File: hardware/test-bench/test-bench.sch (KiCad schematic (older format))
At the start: 34 parts, among them J1 Conn_Mem_Ext, J2 Conn_Reg, J3 SWD, J4 Conn_Mem, J5 FTDI, J6 Conn_Power, SW1 SW_Push_4pin, SW2 SW_Push_4pin, U1 STM32G030F6, U2 MCP23S17_SS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

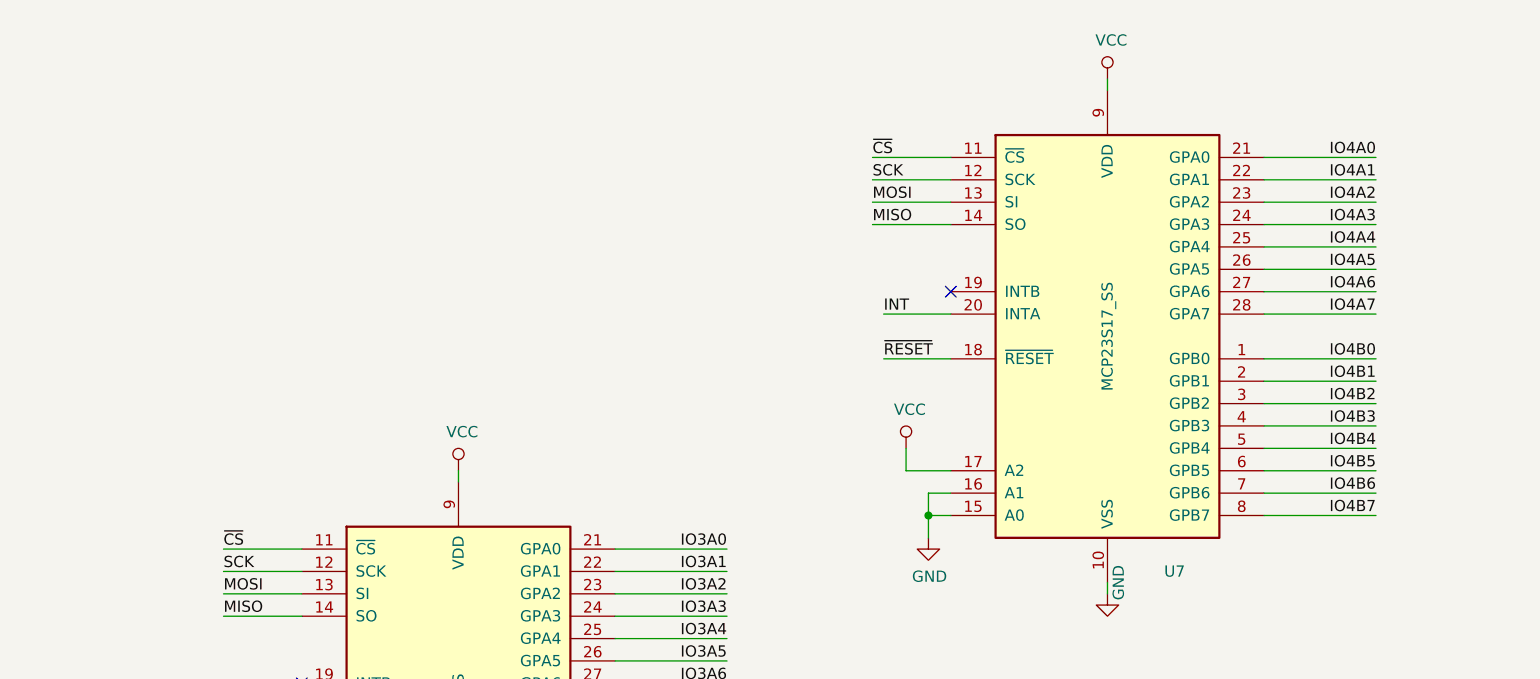
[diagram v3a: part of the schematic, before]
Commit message: Added test points
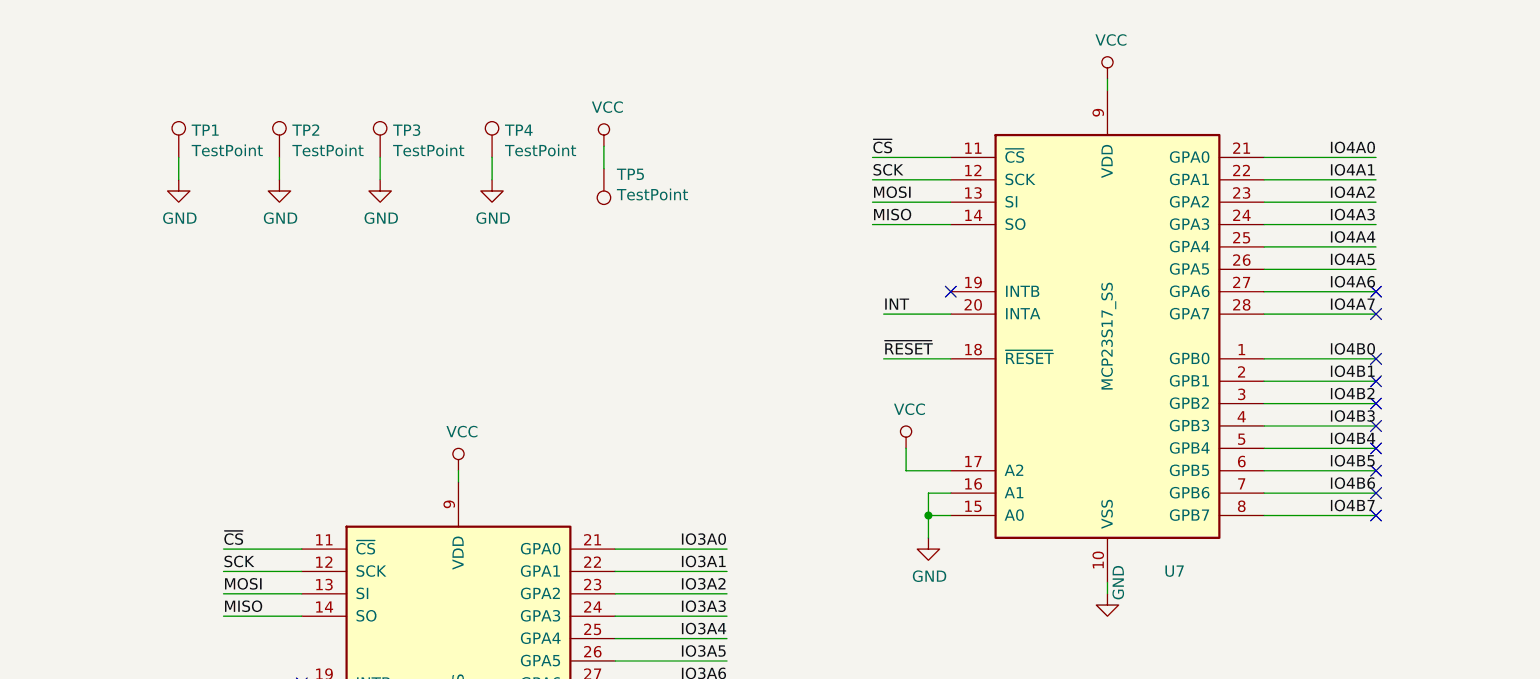
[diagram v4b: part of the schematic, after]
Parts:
- added TP1, TP2, TP3, TP4: TestPoint, TestPoint:TestPoint_THTPad_D2.0mm_Drill1.0mm, symbol Connector:TestPoint
- added TP5: TestPoint, TestPoint:TestPoint_Pad_2.0x2.0mm, symbol Connector:TestPoint
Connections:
- net GND: now also TP1.1, TP2.1, TP3.1, TP4.1
- net VCC: now also TP5.1
- no-connect marks 20 -> 30

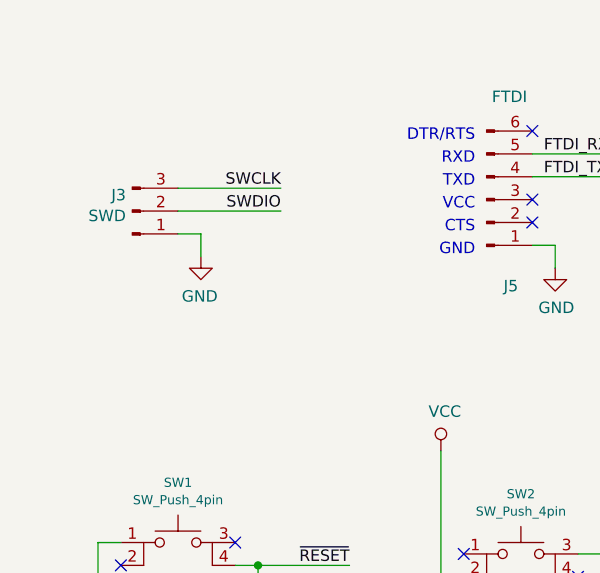
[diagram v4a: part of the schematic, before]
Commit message: Add J-LINK 10-pin SWD header
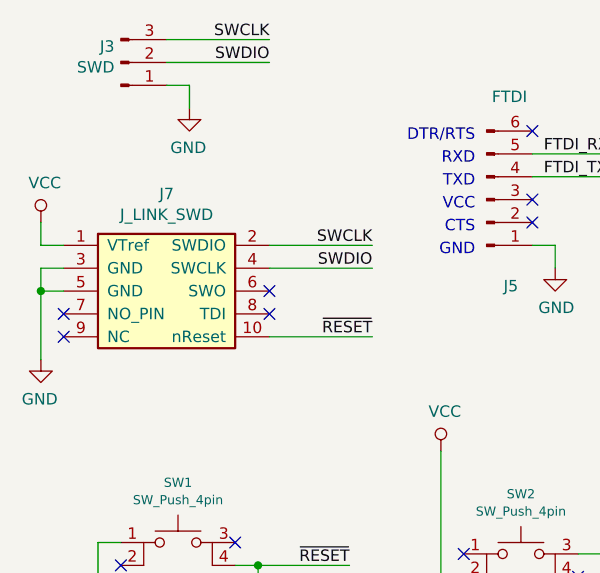
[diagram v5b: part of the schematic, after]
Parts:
- added J7: J_LINK_SWD, Connector_PinHeader_1.27mm:PinHeader_2x05_P1.27mm_Vertical_SMD, symbol riscv-serial:J_LINK_SWD
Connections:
- net GND: now also J7.3 (GND), J7.5 (GND)
- net SWCLK: now also J7.2 (SWDIO)
- net SWDIO: now also J7.4 (SWCLK)
- net VCC: now also J7.1 (VTref)
- net ~RESET: now also J7.10 (nReset)
- no-connect marks 30 -> 34
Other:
- moved on the sheet: J3
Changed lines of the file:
@@
 L Connector:Conn_01x03_Male J3
 U 1 1 5F42A36C
-P 1050 1550
-F 0 "J3" H 1022 1480 50  0000 R CNN
-F 1 "SWD" H 1022 1571 50  0000 R CNN
-F 2 "Connector_PinHeader_2.54mm:PinHeader_1x03_P2.54mm_Vertical" H 1050 1550 50  0001 C CNN
-F 3 "~" H 1050 1550 50  0001 C CNN
-	1    1050 1550
+P 1000 900
+F 0 "J3" H 972 830 50  0000 R CNN
+F 1 "SWD" H 972 921 50  0000 R CNN
+F 2 "Connector_PinHeader_2.54mm:PinHeader_1x03_P2.54mm_Vertical" H 1000 900 50  0001 C CNN
+F 3 "~" H 1000 900 50  0001 C CNN
+	1    1000 900
 	1    0    0    1
 $EndComp
@@
 L power:GND #PWR?
 U 1 1 5F43A491
-P 1350 1750
-F 0 "#PWR?" H 1350 1500 50  0001 C CNN
-F 1 "GND" H 1355 1577 50  0000 C CNN
-F 2 "" H 1350 1750 50  0001 C CNN
-F 3 "" H 1350 1750 50  0001 C CNN
-	1    1350 1750
+P 1300 1100
+F 0 "#PWR?" H 1300 850 50  0001 C CNN
+F 1 "GND" H 1305 927 50  0000 C CNN
+F 2 "" H 1300 1100 50  0001 C CNN
+F 3 "" H 1300 1100 50  0001 C CNN
+	1    1300 1100
 	-1   0    0    -1
 $EndComp
 Wire Wire Line
-	1250 1650 1350 1650
-Wire Wire Line
-	1350 1650 1350 1750
-Wire Wire Line
-	1250 1550 1700 1550
-Wire Wire Line
-	1250 1450 1700 1450
-Text Label 1700 1550 2    50   ~ 0
+	1200 1000 1300 1000
+Wire Wire Line
+	1300 1000 1300 1100
+Wire Wire Line
+	1200 900  1650 900
+Wire Wire Line
+	1200 800  1650 800
+Text Label 1650 900  2    50   ~ 0
 SWDIO
-Text Label 1700 1450 2    50   ~ 0
+Text Label 1650 800  2    50   ~ 0
 SWCLK
 $Comp
@@
 NoConn ~ 15100 3000
 NoConn ~ 15100 3100
+$Comp
+L riscv-serial:J_LINK_SWD J7
+U 1 1 5F4D5DF0
+P 1200 1900
+F 0 "J7" H 1200 2325 50  0000 C CNN
+F 1 "J_LINK_SWD" H 1200 2234 50  0000 C CNN
+F 2 "Connector_PinHeader_1.27mm:PinHeader_2x05_P1.27mm_Vertical_SMD" H 1200 1900 50  0001 C CNN
+F 3 "~" H 1200 1900 50  0001 C CNN
+	1    1200 1900
+	1    0    0    -1
+$EndComp
+Wire Wire Line
+	1650 1800 2100 1800
+Wire Wire Line
+	1650 1700 2100 1700
+Text Label 2100 1800 2    50   ~ 0
+SWDIO
+Text Label 2100 1700 2    50   ~ 0
+SWCLK
+$Comp
+L power:VCC #PWR?
+U 1 1 5F542329
+P 650 1600
+F 0 "#PWR?" H 650 1450 50  0001 C CNN
+F 1 "VCC" H 667 1773 50  0000 C CNN
+F 2 "" H 650 1600 50  0001 C CNN
+F 3 "" H 650 1600 50  0001 C CNN
+	1    650  1600
+	1    0    0    -1
+$EndComp
+Wire Wire Line
+	650  1600 650  1700
+Wire Wire Line
+	650  1700 750  1700
+NoConn ~ 750  2000
+NoConn ~ 750  2100
+NoConn ~ 1650 2000
+NoConn ~ 1650 1900
+$Comp
+L power:GND #PWR?
+U 1 1 5F5F9065
+P 650 2200
+F 0 "#PWR?" H 650 1950 50  0001 C CNN
+F 1 "GND" H 655 2027 50  0000 C CNN
+F 2 "" H 650 2200 50  0001 C CNN
+F 3 "" H 650 2200 50  0001 C CNN
+	1    650  2200
+	-1   0    0    -1
+$EndComp
+Wire Wire Line
+	750  1800 650  1800
+Wire Wire Line
+	650  1800 650  1900
+Wire Wire Line
+	750  1900 650  1900
+Connection ~ 650  1900
+Wire Wire Line
+	650  1900 650  2200
+Text Label 2100 2100 2    50   ~ 0
+~RESET
+Wire Wire Line
+	2100 2100 1650 2100
 $EndSCHEMATC

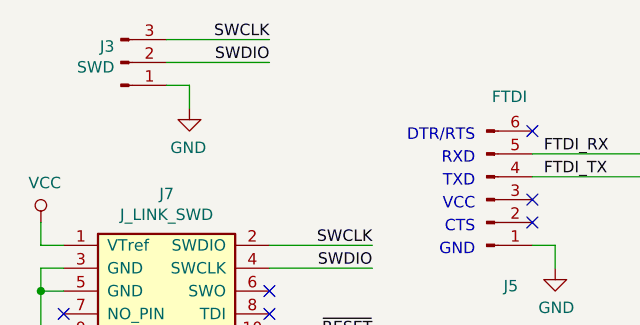
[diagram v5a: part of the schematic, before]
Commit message: Fix SWD pinout
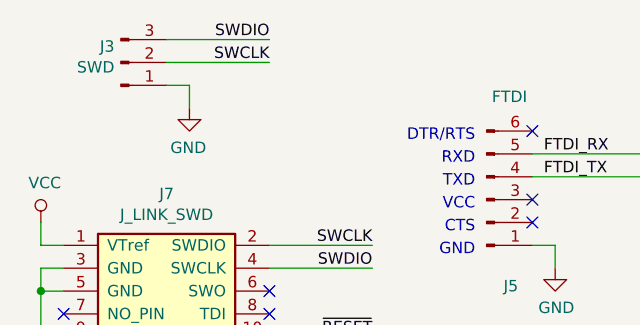
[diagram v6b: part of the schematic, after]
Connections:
- net SWCLK: now also J3.2 (Pin_2); no longer J3.3 (Pin_3)
- net SWDIO: now also J3.3 (Pin_3); no longer J3.2 (Pin_2)
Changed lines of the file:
@@
 $EndComp
-Wire Wire Line
-	1200 1000 1300 1000
 Wire Wire Line
 	1300 1000 1300 1100
 Wire Wire Line
-	1200 900  1650 900
-Wire Wire Line
 	1200 800  1650 800
+Text Label 1650 800  2    50   ~ 0
+SWDIO
 Text Label 1650 900  2    50   ~ 0
-SWDIO
-Text Label 1650 800  2    50   ~ 0
 SWCLK
 $Comp
@@
 Wire Wire Line
 	2100 2100 1650 2100
+Wire Wire Line
+	1200 900  1650 900
+Wire Wire Line
+	1200 1000 1300 1000
 $EndSCHEMATC

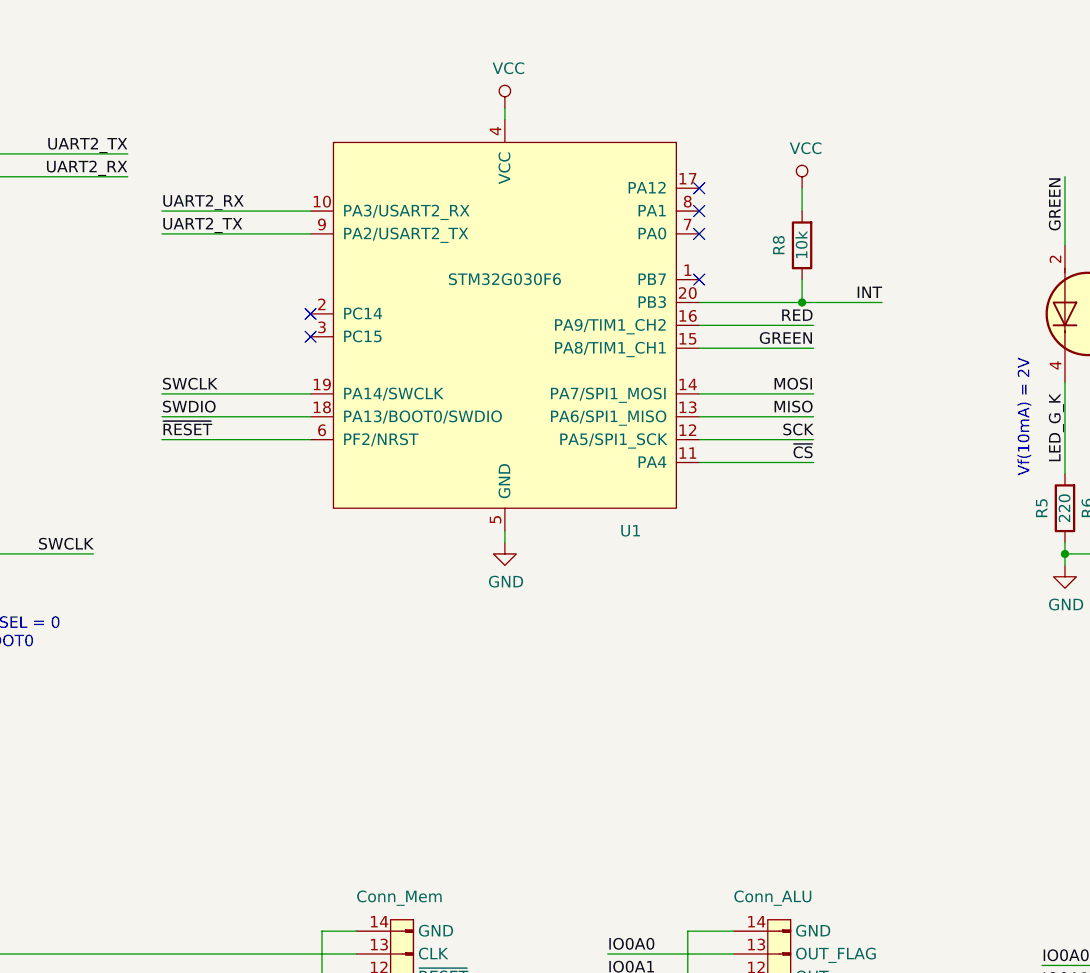
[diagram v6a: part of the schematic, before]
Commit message: Added resistors to some unused pins and a logo
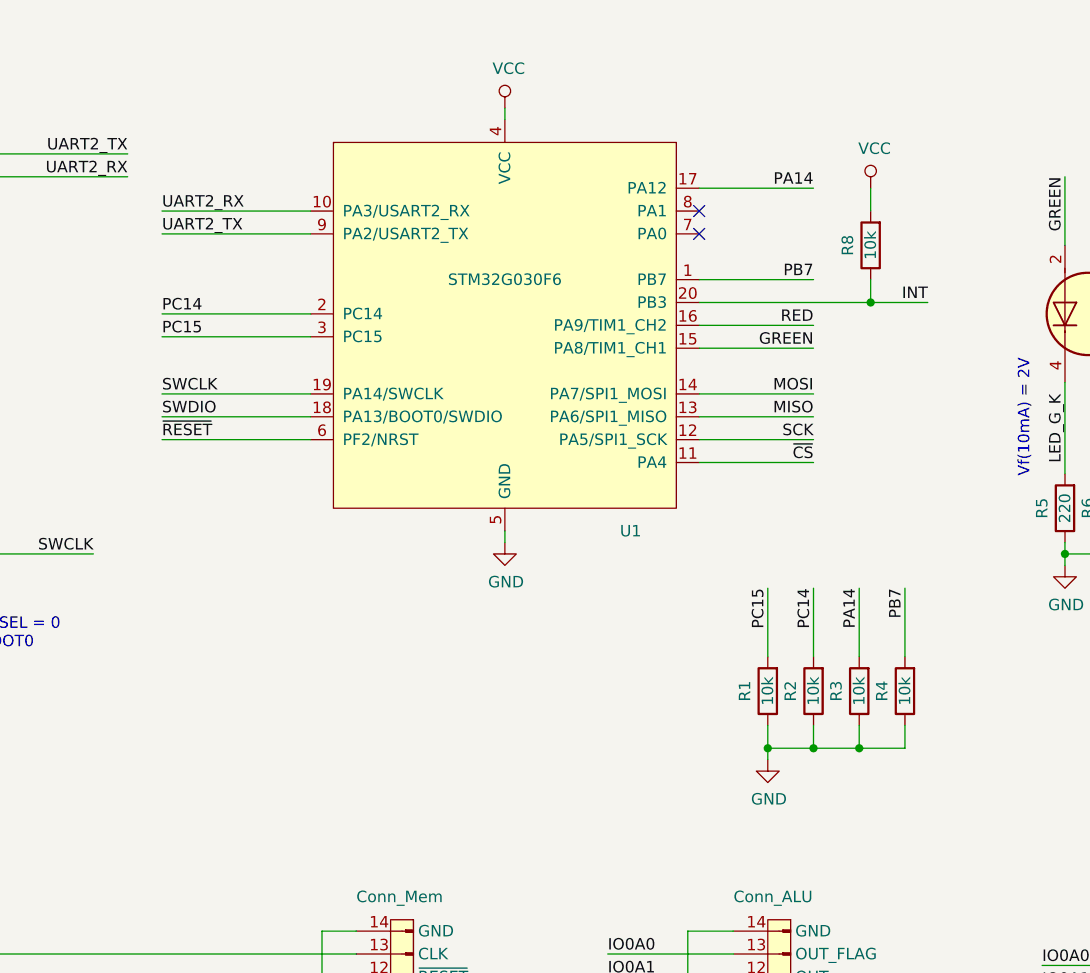
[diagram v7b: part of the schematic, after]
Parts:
- added R1, R2, R3, R4: 10k, Resistor_SMD:R_0805_2012Metric_Pad1.15x1.40mm_HandSolder, symbol Device:R
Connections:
- net GND: now also R1.1, R2.1, R3.1, R4.1
- net PB7: now reaches U1.1 (PB7)
- net PB7: now also R4.2
- net PA14: now reaches U1.17 (PA12)
- net PA14: now also R3.2
- net PC14: now reaches U1.2 (PC14)
- net PC14: now also R2.2
- net PC15: now reaches U1.3 (PC15)
- net PC15: now also R1.2
- no-connect marks 34 -> 30
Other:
- moved on the sheet: R8
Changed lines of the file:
@@
 NoConn ~ 2500 6100
 NoConn ~ 2500 6200
-NoConn ~ 4500 2000
-NoConn ~ 4500 2100
 NoConn ~ 6200 1650
 NoConn ~ 6200 1550
-NoConn ~ 6200 1450
 $Comp
 L Device:LED_Dual_AACC D4
@@
 INT
 Wire Wire Line
-	6200 1950 6650 1950
-Text Label 7000 1950 2    50   ~ 0
+	6200 1950 6950 1950
+Text Label 7200 1950 2    50   ~ 0
 INT
-NoConn ~ 6200 1850
 $Comp
 L Device:R R8
 U 1 1 5F0F7764
-P 6650 1700
-F 0 "R8" V 6750 1700 50  0000 C CNN
-F 1 "10k" V 6650 1700 50  0000 C CNN
-F 2 "Resistor_SMD:R_0805_2012Metric_Pad1.15x1.40mm_HandSolder" V 6580 1700 50  0001 C CNN
-F 3 "~" H 6650 1700 50  0001 C CNN
-	1    6650 1700
+P 6950 1700
+F 0 "R8" V 7050 1700 50  0000 C CNN
+F 1 "10k" V 6950 1700 50  0000 C CNN
+F 2 "Resistor_SMD:R_0805_2012Metric_Pad1.15x1.40mm_HandSolder" V 6880 1700 50  0001 C CNN
+F 3 "~" H 6950 1700 50  0001 C CNN
+	1    6950 1700
 	-1   0    0    1
 $EndComp
 Wire Wire Line
-	6650 1850 6650 1950
-Connection ~ 6650 1950
-Wire Wire Line
-	6650 1950 7000 1950
+	6950 1850 6950 1950
+Connection ~ 6950 1950
+Wire Wire Line
+	6950 1950 7200 1950
 $Comp
 L power:VCC #PWR?
 U 1 1 5F116DD9
-P 6650 1450
-F 0 "#PWR?" H 6650 1300 50  0001 C CNN
-F 1 "VCC" H 6667 1623 50  0000 C CNN
-F 2 "" H 6650 1450 50  0001 C CNN
-F 3 "" H 6650 1450 50  0001 C CNN
-	1    6650 1450
-	1    0    0    -1
-$EndComp
-Wire Wire Line
-	6650 1450 6650 1550
+P 6950 1450
+F 0 "#PWR?" H 6950 1300 50  0001 C CNN
+F 1 "VCC" H 6967 1623 50  0000 C CNN
+F 2 "" H 6950 1450 50  0001 C CNN
+F 3 "" H 6950 1450 50  0001 C CNN
+	1    6950 1450
+	1    0    0    -1
+$EndComp
+Wire Wire Line
+	6950 1450 6950 1550
 Wire Wire Line
 	2800 1300 3700 1300
@@
 Wire Wire Line
 	1200 1000 1300 1000
+$Comp
+L Device:R R3
+U 1 1 5EF2C377
+P 6900 3650
+F 0 "R3" V 7000 3650 50  0000 C CNN
+F 1 "10k" V 6900 3650 50  0000 C CNN
+F 2 "Resistor_SMD:R_0805_2012Metric_Pad1.15x1.40mm_HandSolder" V 6830 3650 50  0001 C CNN
+F 3 "~" H 6900 3650 50  0001 C CNN
+	1    6900 3650
+	-1   0    0    1
+$EndComp
+$Comp
+L Device:R R4
+U 1 1 5EF2C481
+P 7100 3650
+F 0 "R4" V 7200 3650 50  0000 C CNN
+F 1 "10k" V 7100 3650 50  0000 C CNN
+F 2 "Resistor_SMD:R_0805_2012Metric_Pad1.15x1.40mm_HandSolder" V 7030 3650 50  0001 C CNN
+F 3 "~" H 7100 3650 50  0001 C CNN
+	1    7100 3650
+	-1   0    0    1
+$EndComp
+Wire Wire Line
+	4500 2000 3850 2000
+Text Label 3850 2000 0    50   ~ 0
+PC14
+Text Label 3850 2100 0    50   ~ 0
+PC15
+Wire Wire Line
+	3850 2100 4500 2100
+Wire Wire Line
+	6200 1850 6700 1850
+Text Label 6700 1850 2    50   ~ 0
+PB7
+Text Label 6700 1450 2    50   ~ 0
+PA14
+Wire Wire Line
+	6700 1450 6200 1450
+Text Label 7100 3200 3    50   ~ 0
+PB7
+Text Label 6900 3200 3    50   ~ 0
+PA14
+Text Label 6500 3200 3    50   ~ 0
+PC15
+Text Label 6700 3200 3    50   ~ 0
+PC14
+$Comp
+L Device:R R1
+U 1 1 5F0B4023
+P 6500 3650
+F 0 "R1" V 6600 3650 50  0000 C CNN
+F 1 "10k" V 6500 3650 50  0000 C CNN
+F 2 "Resistor_SMD:R_0805_2012Metric_Pad1.15x1.40mm_HandSolder" V 6430 3650 50  0001 C CNN
+F 3 "~" H 6500 3650 50  0001 C CNN
+	1    6500 3650
+	-1   0    0    1
+$EndComp
+$Comp
+L Device:R R2
+U 1 1 5F0B402A
+P 6700 3650
+F 0 "R2" V 6800 3650 50  0000 C CNN
+F 1 "10k" V 6700 3650 50  0000 C CNN
+F 2 "Resistor_SMD:R_0805_2012Metric_Pad1.15x1.40mm_HandSolder" V 6630 3650 50  0001 C CNN
+F 3 "~" H 6700 3650 50  0001 C CNN
+	1    6700 3650
+	-1   0    0    1
+$EndComp
+Wire Wire Line
+	7100 3500 7100 3200
+Wire Wire Line
+	6900 3500 6900 3200
+Wire Wire Line
+	6700 3500 6700 3200
+Wire Wire Line
+	6500 3500 6500 3200
+Wire Wire Line
+	6500 3800 6500 3900
+Wire Wire Line
+	6500 3900 6700 3900
+Wire Wire Line
+	7100 3900 7100 3800
+Wire Wire Line
+	6900 3800 6900 3900
+Connection ~ 6900 3900
+Wire Wire Line
+	6900 3900 7100 3900
+Wire Wire Line
+	6700 3800 6700 3900
+Connection ~ 6700 3900
+Wire Wire Line
+	6700 3900 6900 3900
+$Comp
+L power:GND #PWR?
+U 1 1 5F246B69
+P 6500 3950
+F 0 "#PWR?" H 6500 3700 50  0001 C CNN
+F 1 "GND" H 6505 3777 50  0000 C CNN
+F 2 "" H 6500 3950 50  0001 C CNN
+F 3 "" H 6500 3950 50  0001 C CNN
+	1    6500 3950
+	1    0    0    -1
+$EndComp
+Wire Wire Line
+	6500 3950 6500 3900
+Connection ~ 6500 3900
 $EndSCHEMATC
